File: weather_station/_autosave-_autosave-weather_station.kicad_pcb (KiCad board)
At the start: 2 copper layers, 64.8 x 69.9 mm, 17 parts, among them J1 RJ11-6, J2 RJ11-6, J3 1935161, U1 BME280, U2 ESP32-DEVKITC-32D

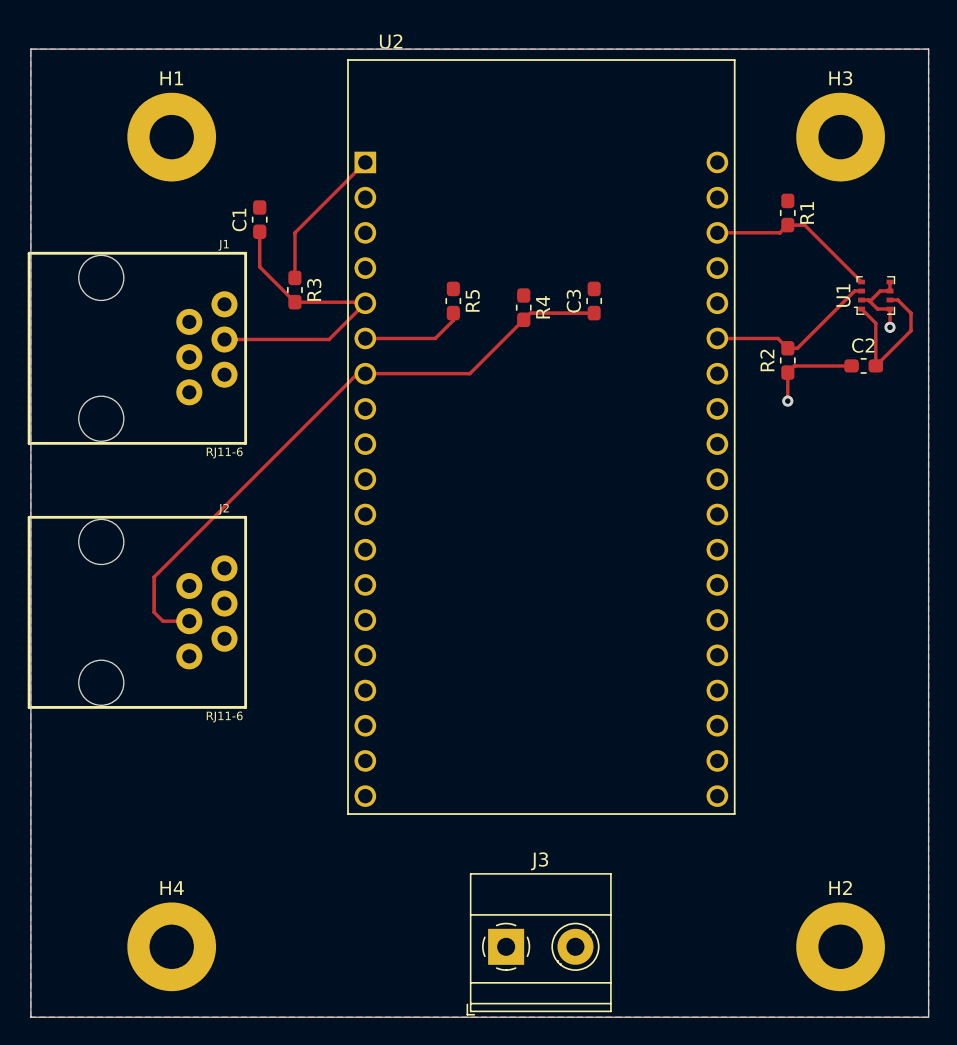
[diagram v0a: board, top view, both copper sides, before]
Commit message: pcb updates, dont use this the schematic is scuffed
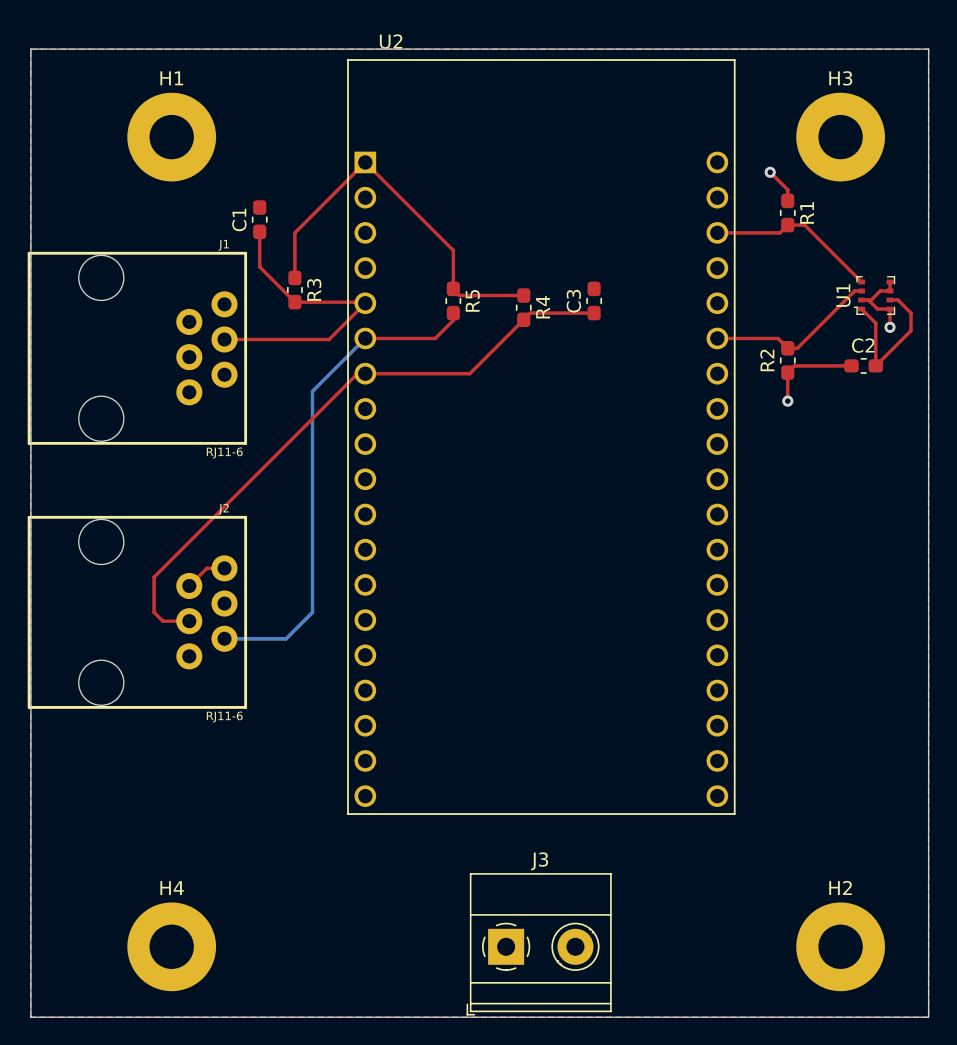
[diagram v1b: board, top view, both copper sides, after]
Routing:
- net /WIND_DIR: track 7.42 -> 35.9 mm
- net VDD: track 23.3 -> 43.0 mm, vias 2 -> 3
- net GND: track 11.3 -> 14.4 mm
